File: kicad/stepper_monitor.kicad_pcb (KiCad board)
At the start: 2 copper layers, 38.5 x 43 mm, 58 parts, among them J1 Conn_01x04_Pin, J2 Conn_01x04_Pin, J3 Conn_01x02_Pin, J4 USB_C_Receptacle_USB2.0, J5 JTAG, Q1 MMDT2222A, SW1 SW_Push, U1 5V, U2 CP2102N-A01-GQFN28, U3 AMS1117-3.3, U4 CC6920BSO-5A, U5 CC6920BSO-5A, U6 ESP32-WROOM-32U-N4

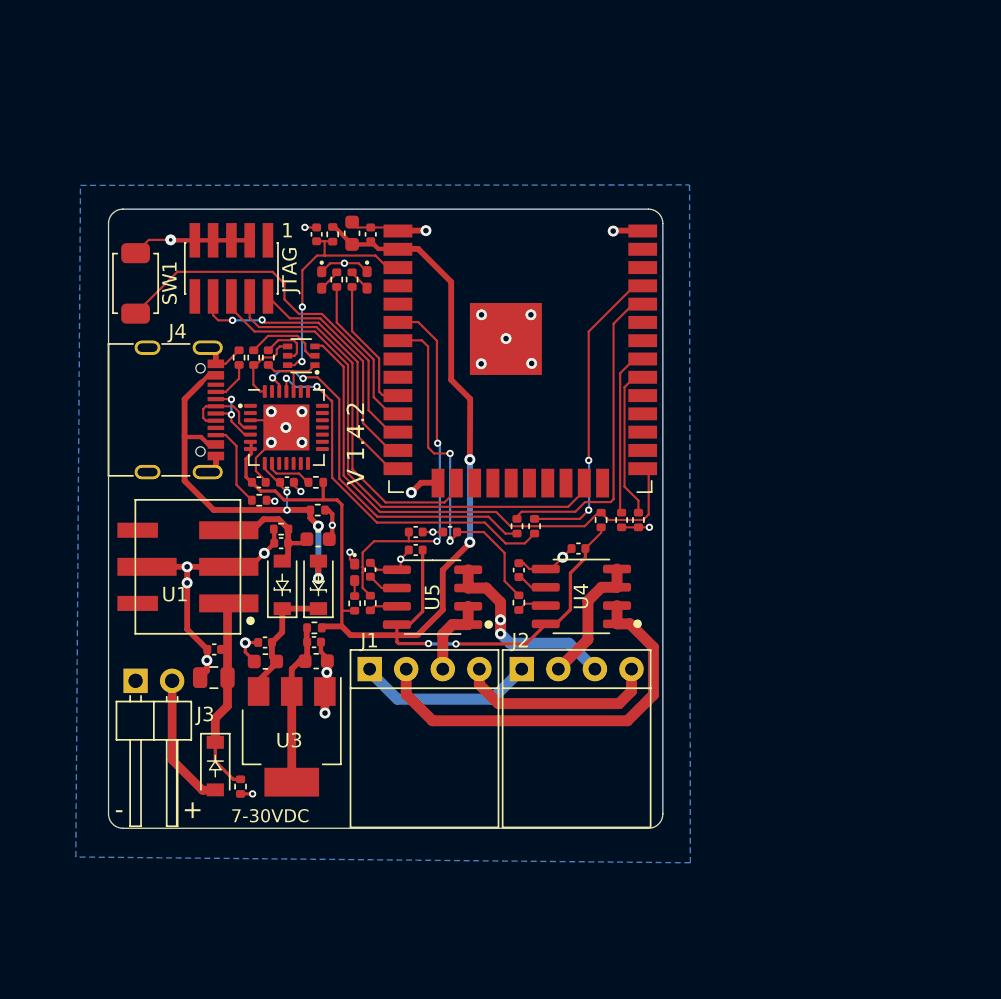
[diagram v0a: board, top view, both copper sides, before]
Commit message: V3D improvements (#1)
- M3 corner holes
- JST XH connectors
- Match JLCPCB capabilities
- increased board size
- increased via size
- adjusted tracks in some locations to match capabilities
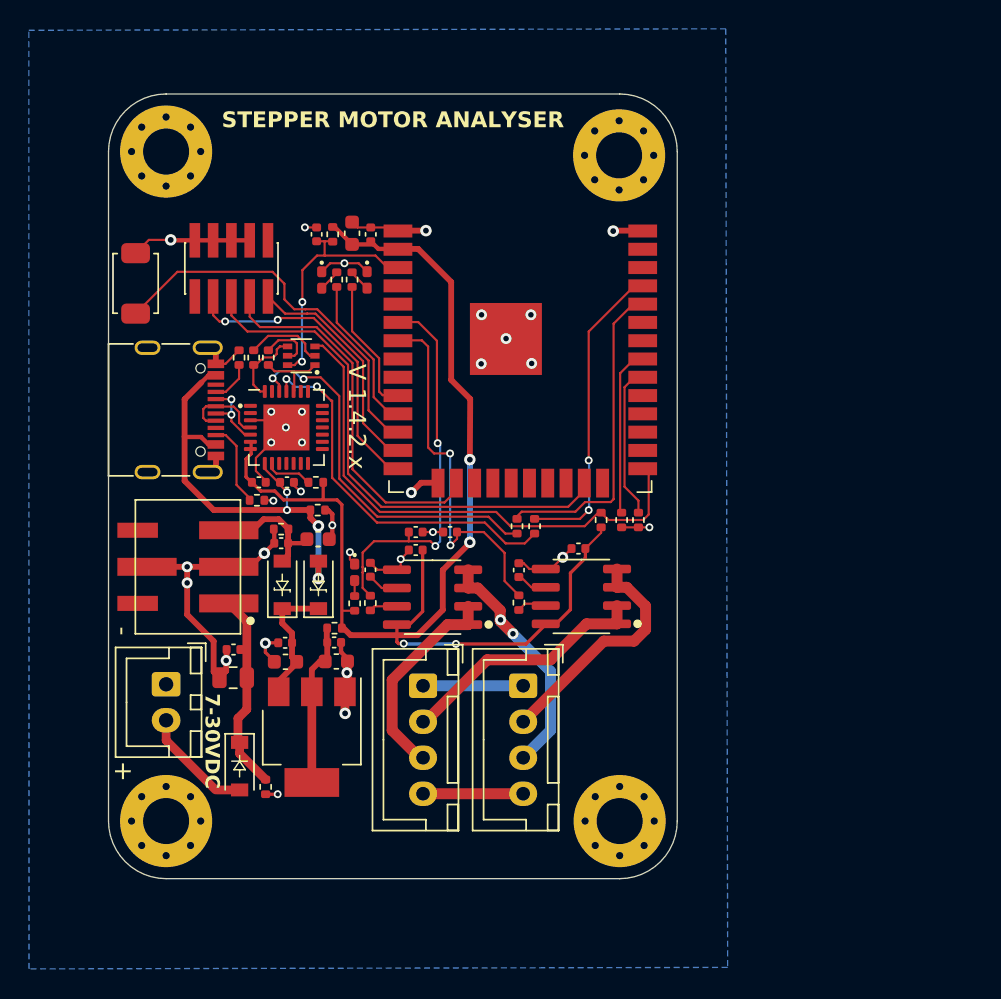
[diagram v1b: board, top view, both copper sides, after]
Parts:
- added H1: MountingHole, MountingHole:MountingHole_3.2mm_M3_Pad_Via, F.Cu at (4.00, -47.0)
- added H2: MountingHole, MountingHole:MountingHole_3.2mm_M3_Pad_Via, F.Cu at (35.5, -46.7)
- added H3: MountingHole, MountingHole:MountingHole_3.2mm_M3_Pad_Via, F.Cu at (4.00, -0.50)
- added H4: MountingHole, MountingHole:MountingHole_3.2mm_M3_Pad_Via, F.Cu at (35.5, -0.50)
- J1, J2: footprint stepper_monitor:connector_4pins_horizontal -> Connector_JST:JST_XH_B4B-XH-A_1x04_P2.50mm_Vertical
- J3: footprint stepper_monitor:PinHeader_1x02_P2.54mm_Horizontal_JLCPCB -> Connector_JST:JST_XH_B2B-XH-A_1x02_P2.50mm_Vertical
- moved J2 3.89 mm to (28.8, -9.90), turned to -90 degrees
- moved R3 1.74 mm to (10.9, -2.87)
- moved D3 1.69 mm to (9.11, -4.31)
- moved C10 1.39 mm to (15.8, -11.6)
- moved C11 1.39 mm to (15.7, -12.9)
- moved C6 1.39 mm to (12.3, -11.6)
- moved C8 1.39 mm to (12.3, -12.9)
- moved R16 1.39 mm to (15.7, -13.9)
- moved U3 1.39 mm to (14.1, -6.33)
- moved C2 1.34 mm to (8.68, -12.4)
- moved C1 1.34 mm to (8.66, -10.5)
- moved J1 1.16 mm to (21.8, -9.90), turned to -90 degrees
- moved J3 0.88 mm to (4.00, -10.0), turned to -90 degrees
- moved R5 0.15 mm to (10.3, -22.8)
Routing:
- net Net-(J1-Pin_2): track 28.2 -> 16.8 mm
- net Net-(J1-Pin_3): track 5.74 -> 14.6 mm
- net Net-(J2-Pin_2): track 9.27 -> 16.6 mm
- net Net-(J1-Pin_4): track 14.1 -> 6.96 mm
- net Net-(J1-Pin_1): track 12.4 -> 6.96 mm
- net Net-(J2-Pin_3): track 14.6 -> 17.9 mm
- net GNDD: track 77.7 -> 79.9 mm
- net Net-(D3-A): track 9.46 -> 7.81 mm
- net +3V3: track 91.2 -> 89.8 mm
- net CHB: track 25.2 -> 25.8 mm
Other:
- board size 38.5 x 43 mm -> 39.5 x 54.5 mm
- board text added: "ESP32,OSH,github/zapta"
- board text added: "JLCJLCJLCJLC"
- board text added: "STEPPER MOTOR ANALYSER"
- board text added: "V 1.4.2.x"
- board text removed: "1"
- board text removed: "STEPPER MOTOR ANALYZER ESP32, OSH, github/zapta"
- board text removed: "V 1.4.2"

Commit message: Current sensors between the connectors
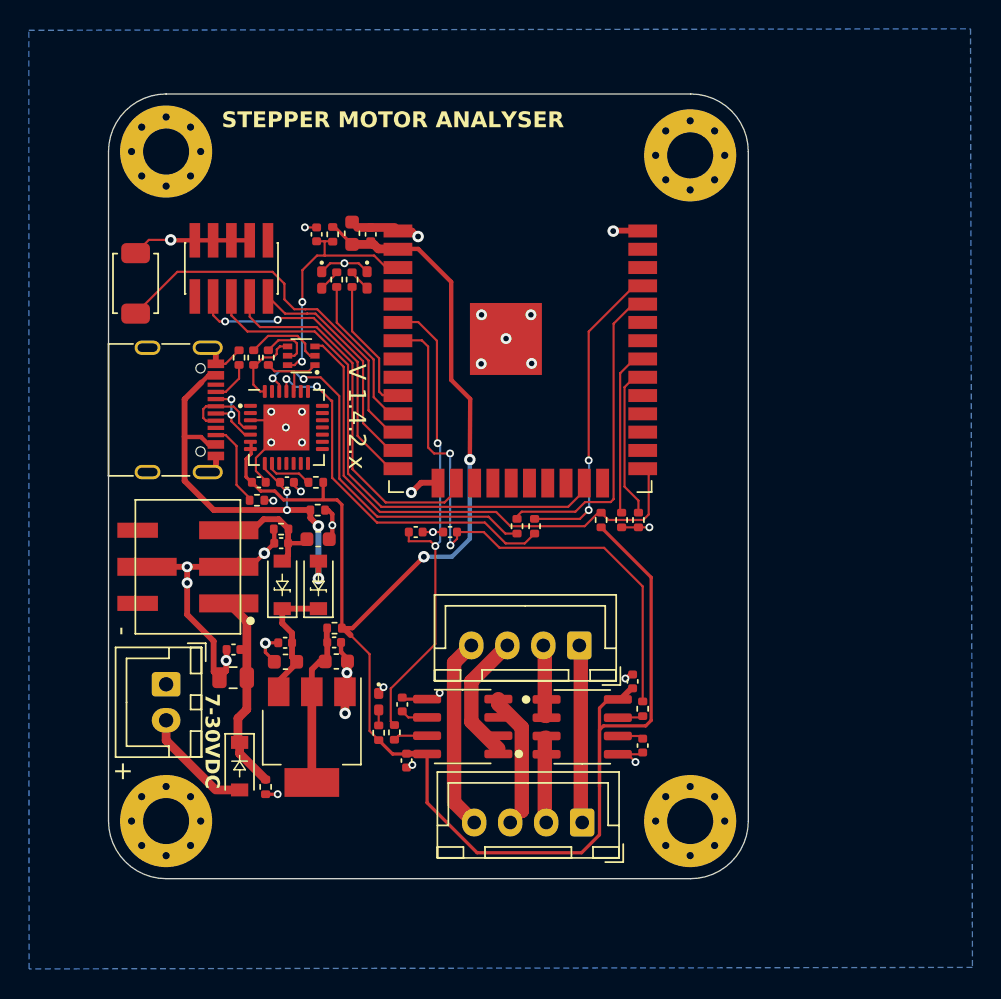
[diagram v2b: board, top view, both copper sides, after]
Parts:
- moved C15 14.9 mm to (37.1, -5.74), turned to 90 degrees
- moved C17 14.6 mm to (20.7, -4.70), turned to 90 degrees
- moved R19 11.3 mm to (37.1, -8.30)
- moved J1 11.2 mm to (32.7, -12.7), turned to 180 degrees
- moved J2 10.3 mm to (32.9, -0.40), turned to 180 degrees
- moved C14 9.97 mm to (36.4, -10.2), turned to -90 degrees
- moved C18 9.61 mm to (20.4, -8.60)
- moved U5 9.23 mm to (24.6, -7.07)
- moved D4 9.14 mm to (18.8, -8.79)
- moved R20 9.14 mm to (19.9, -6.66)
- moved R6 9.14 mm to (18.8, -6.63)
- moved U4 9.06 mm to (32.9, -7.04), turned to -90 degrees
- moved H2 4.93 mm to (40.4, -46.7)
- moved H4 4.90 mm to (40.4, -0.50)
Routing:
- net +3V3: track 89.8 -> 123.7 mm, vias 4 -> 2
- net CHB: track 25.8 -> 41.0 mm
- net Net-(J1-Pin_2): track 16.8 -> 4.97 mm
- net Net-(J2-Pin_2): track 16.6 -> 6.10 mm
- net Net-(J2-Pin_3): track 17.9 -> 9.58 mm, vias 2 -> 0
- net CHA: track 27.1 -> 34.2 mm
- net Net-(J1-Pin_4): track 6.96 -> 13.4 mm
- net Net-(J1-Pin_3): track 14.6 -> 8.99 mm
- net Net-(J1-Pin_1): track 6.96 -> 12.4 mm
- net GNDD: track 79.9 -> 77.0 mm, vias 32 -> 34
- net EN: track 17.8 -> 16.3 mm
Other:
- board size 39.5 x 54.5 mm -> 44.4 x 54.5 mm
- board text removed: "ESP32,OSH,github/zapta"

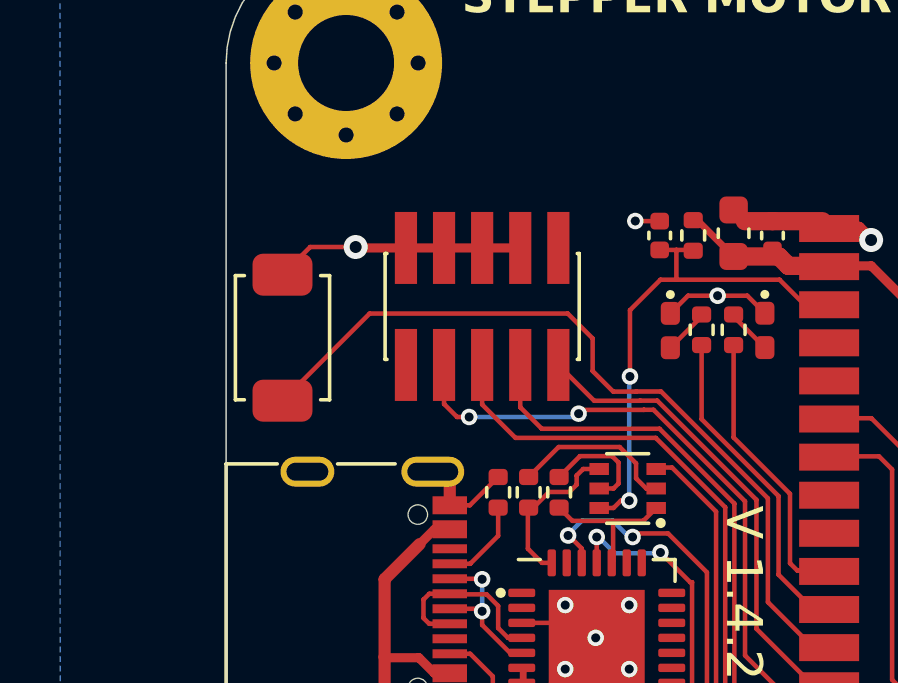
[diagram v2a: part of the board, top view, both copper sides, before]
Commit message: JLC basic part button
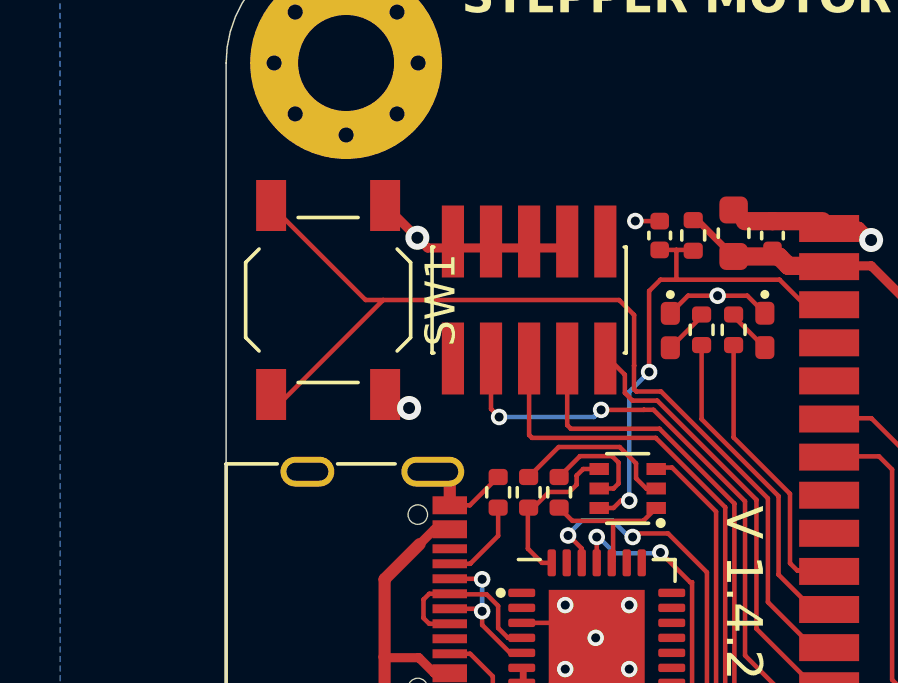
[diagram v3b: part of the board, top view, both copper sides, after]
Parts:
- SW1: footprint stepper_monitor:SW_Push_SPST_NO_Alps_SKRK -> Button_Switch_SMD:SW_SPST_TL3342
- moved SW1 1.97 mm to (3.40, -39.1)
- moved J5 1.58 mm to (10.1, -39.1)
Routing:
- net SWITCH: track 26.7 -> 32.9 mm
- net GNDD: track 77.0 -> 75.4 mm, vias 34 -> 35
- net ESP_TDI: track 21.8 -> 20.5 mm
- net ESP_TMS: track 16.0 -> 14.8 mm
- net ESP_TCK: track 26.3 -> 25.3 mm
- net ESP_TDO: track 36.8 -> 36.0 mm

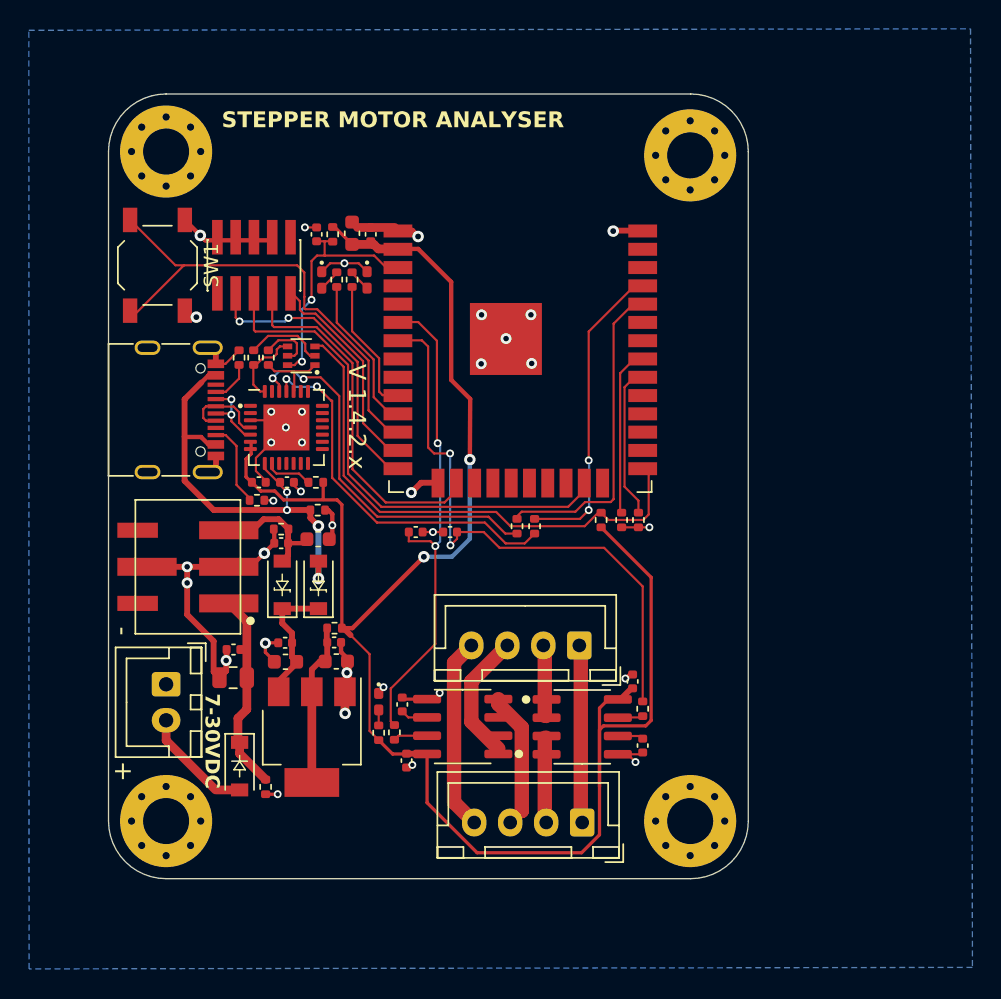
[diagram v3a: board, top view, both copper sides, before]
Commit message: Connected VZCR pin from CC6920BSO. Added big scope test points. Ignored local file.
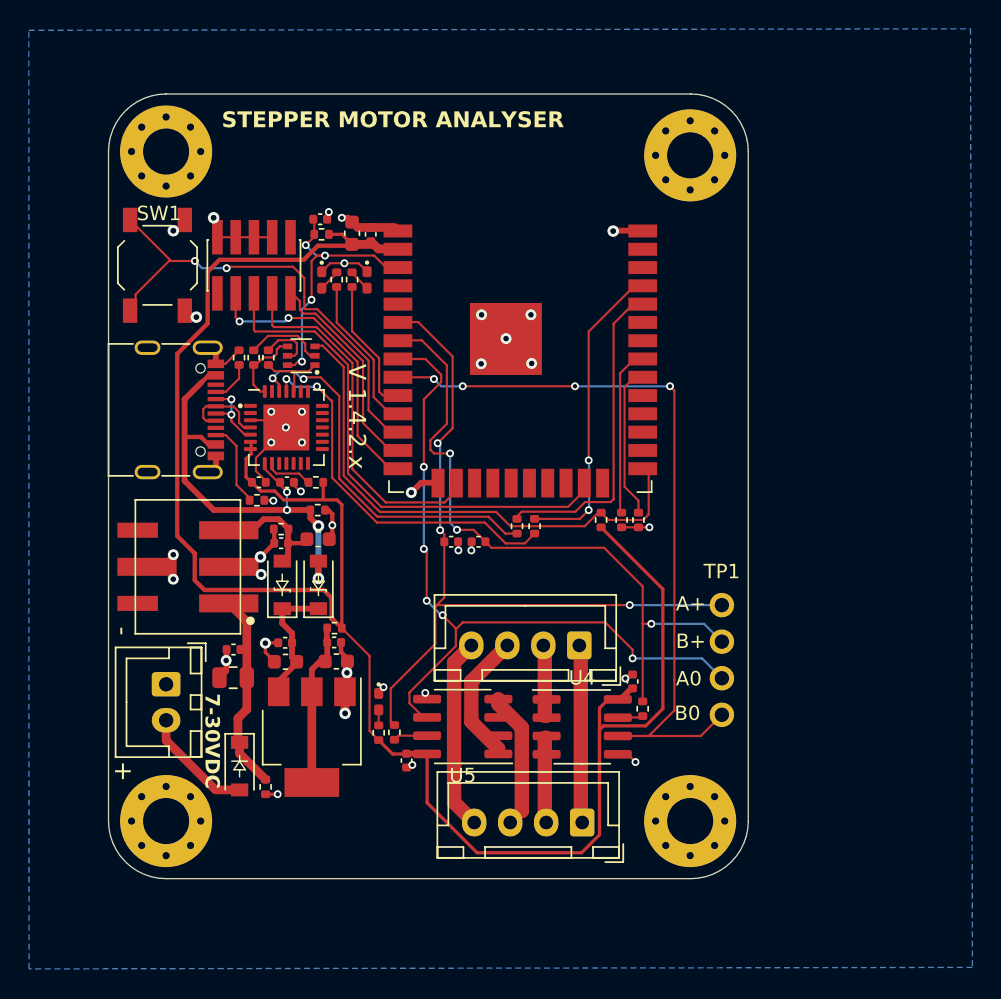
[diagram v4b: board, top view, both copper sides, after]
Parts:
- removed C15, C18: DNP, Capacitor_SMD:C_0402_1005Metric
- added TP1: ScopeTestPoint, Connector_PinHeader_2.54mm:PinHeader_1x04_P2.54mm_Vertical, F.Cu at (42.6, -15.5)
- U4, U5: footprint stepper_monitor:SOIC-8_3.9x4.9mm_P1.27mm -> Package_SO:SOIC-8_3.9x4.9mm_P1.27mm
- moved C19 2.55 mm to (23.8, -19.9)
- moved C16 2.09 mm to (25.7, -19.9)
- moved C9 1.08 mm to (14.7, -42.3), turned to 180 degrees
- moved R12 0.77 mm to (14.8, -41.3), turned to 0 degrees
- turned U4 to 0 degrees
- turned U5 to 180 degrees
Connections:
- U4 pad 6: Net-(U4-NC) -> CHB_V0
- U5 pad 6: Net-(U5-NC) -> CHA_V0
- U6 pad 8: unconnected-(U6-IO32-Pad8) -> CHA_V0
- U6 pad 9: unconnected-(U6-IO33-Pad9) -> CHB_V0
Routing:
- net CHB_V0: track 0.00 -> 54.3 mm, vias 0 -> 4
- net CHA_V0: track 0.00 -> 51.4 mm, vias 0 -> 5
- net CHA: track 34.2 -> 52.6 mm, vias 2 -> 3
- net GNDD: track 75.4 -> 58.9 mm, vias 35 -> 38
- net +3V3: track 123.7 -> 136.2 mm, vias 2 -> 0
- net CHB: track 41.0 -> 46.0 mm, vias 2 -> 3
- net Net-(U5-NC): track 1.90 -> 0.00 mm
- net EN: track 16.3 -> 18.2 mm, vias 2 -> 4
- net Net-(U4-NC): track 1.80 -> 0.00 mm
- net SWITCH: track 32.9 -> 32.8 mm, vias 0 -> 2
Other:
- board text added: "A+"
- board text added: "A0"
- board text added: "B+"
- board text added: "B0"
